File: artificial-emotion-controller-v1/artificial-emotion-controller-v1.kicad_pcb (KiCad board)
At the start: 2 copper layers, 66.5 x 86.5 mm, 31 parts, among them J1 28BYJ-48 5-pin, J2 5V screw terminal, J8 I2C 3V3, U1 ESP32-S3 SuperMini, U2 ULN2003A

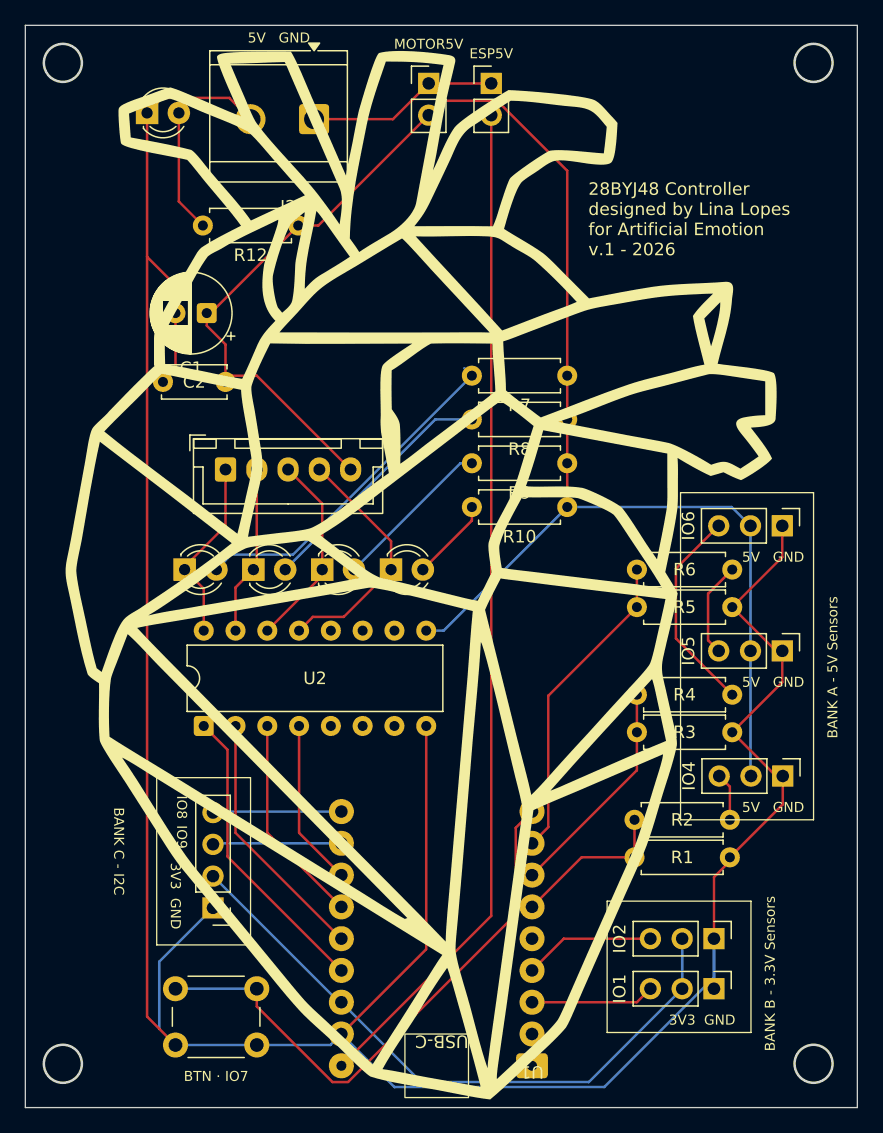
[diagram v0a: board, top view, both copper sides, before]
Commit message: Revise controller v1 sensor banks, GPIO map, and fabrication files.
Bank A is now four 3.3V ports; the 5V divider is a single Bank B input.

Co-authored-by: Cursor <cursoragent@cursor.com>
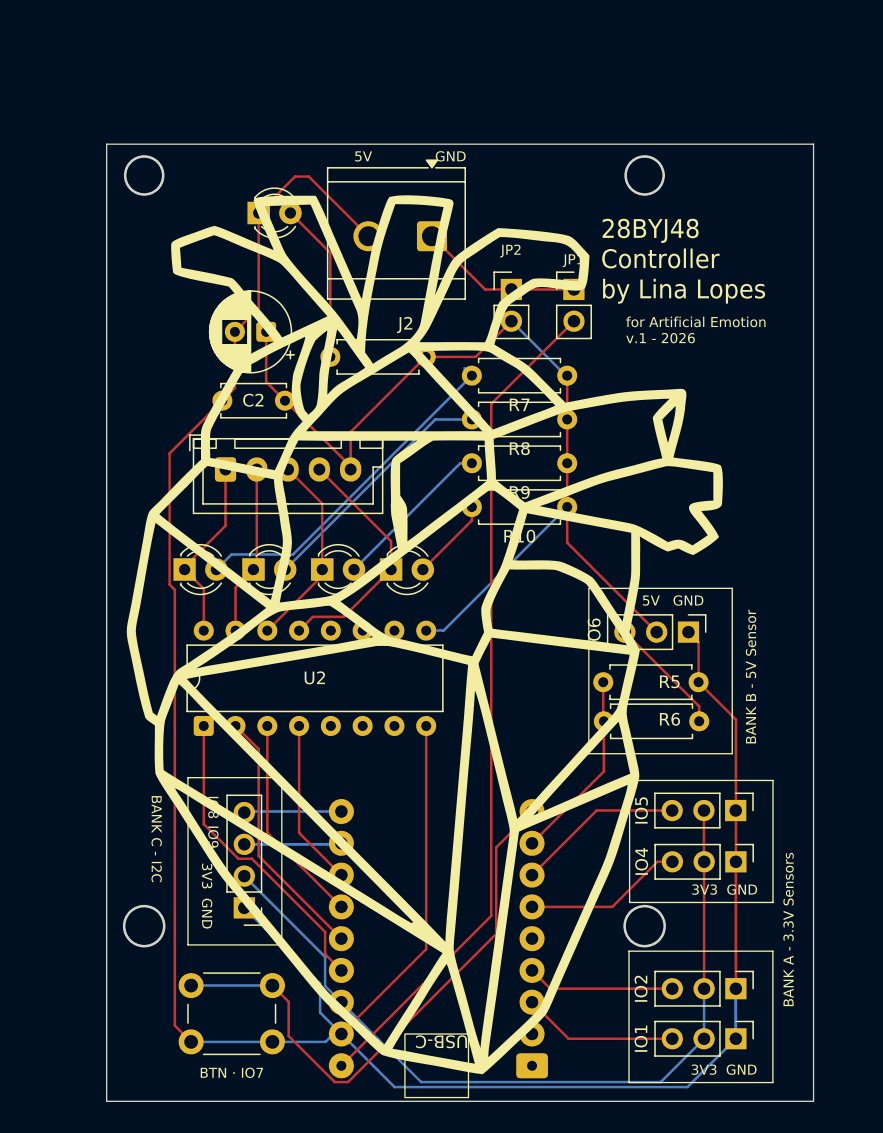
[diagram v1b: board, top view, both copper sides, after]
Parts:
- removed R1, R3: 15K, Resistor_THT:R_Axial_DIN0207_L6.3mm_D2.5mm_P7.62mm_Horizontal
- removed R2, R4: 10K, Resistor_THT:R_Axial_DIN0207_L6.3mm_D2.5mm_P7.62mm_Horizontal
- IO1: value SENSOR B1 3V3 -> SENSOR A1 3V3
- IO2: value SENSOR B2 3V3 -> SENSOR A2 3V3
- IO4: value SENSOR A1 5V -> SENSOR A3 3V3
- IO5: renamed from IO6; value SENSOR A2 5V -> SENSOR A4 3V3
- IO6: renamed from IO5; value SENSOR A3 5V -> SENSOR 5V
- moved IO5 23.1 mm to (129.8, 99.8)
- moved JP1 17.7 mm to (116.8, 58.1)
- moved JP2 17.7 mm to (111.8, 58.1)
- moved R12 14.6 mm to (105.0, 63.5)
- moved J2 13.3 mm to (105.5, 53.9)
- moved R6 12.4 mm to (126.9, 92.6)
- moved D5 12.0 mm to (91.7, 52.0)
- moved IO4 7.81 mm to (129.8, 103.9)
- moved IO6 7.65 mm to (126.0, 85.5)
- moved R5 6.58 mm to (126.8, 89.5)
- moved C1 4.98 mm to (92.2, 61.5)
- moved C2 4.98 mm to (93.8, 67.0)
- moved IO1 4.37 mm to (129.8, 118.0)
- moved IO2 4.37 mm to (129.8, 114.0)
- moved J8 2.50 mm to (90.5, 107.5)
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- renumbered ESP5V to JP1, MOTOR5V to JP2
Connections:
- net /ADC_A3 renamed /SENSOR_B1_ADC
- net /SENSOR_B1 renamed /SENSOR_A1
- net /SENSOR_B2 renamed /SENSOR_A2
- IO4 pad 2: /5V_MOTOR -> /3V3
- IO4 pad 3: Net-(J3-Pin_3) -> /SENSOR_A3
- IO5 pad 2: /5V_MOTOR -> /3V3
- IO5 pad 3: Net-(J4-Pin_3) -> /SENSOR_A4
- U1 pad 6: /ADC_A1 -> /SENSOR_A3
- U1 pad 7: /ADC_A2 -> /SENSOR_A4
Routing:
- net /5V_MOTOR: track 135.1 -> 78.4 mm
- net /GND: track 235.4 -> 207.6 mm
- net /ADC_A2: track 17.9 -> 0.00 mm
- net Net-(J4-Pin_3): track 16.8 -> 0.00 mm
- net /ESP_5V: track 80.9 -> 67.2 mm
- net /3V3: track 51.4 -> 64.8 mm
- net /SENSOR_A4: track 0.00 -> 13.3 mm
- net /ADC_A1: track 12.8 -> 0.00 mm
- net /SENSOR_A3: track 0.00 -> 12.7 mm
- net /SENSOR_B1_ADC: track 25.4 -> 15.3 mm
- net Net-(J3-Pin_3): track 3.85 -> 0.00 mm
- net Net-(D5-A): track 9.80 -> 12.8 mm
- net /SENSOR_A1: track 9.91 -> 12.4 mm
- net /I2C_SDA: track 10.4 -> 7.91 mm
- net /I2C_SCL: track 10.4 -> 8.02 mm
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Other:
- board size 66.5 x 86.5 mm -> 56.5 x 76.5 mm
- board text added: "28BYJ48 Controller by Lina Lopes"
- board text added: "BANK A - 3.3V Sensors"
- board text added: "BANK B - 5V Sensor"
- board text added: "for Artificial Emotion v.1 - 2026"
- board text removed: "28BYJ48 Controller designed by Lina Lopes for Artificial Emotion v.1 - 2026"
- board text removed: "BANK A - 5V Sensors"
- board text removed: "BANK B - 3.3V Sensors"
